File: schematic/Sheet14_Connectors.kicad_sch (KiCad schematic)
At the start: 5 parts, among them J2 JESD_DEBUG, J3 SPW_PORT1, J4 SPW_PORT2, J5 JTAG, J6 SPI_DEBUG

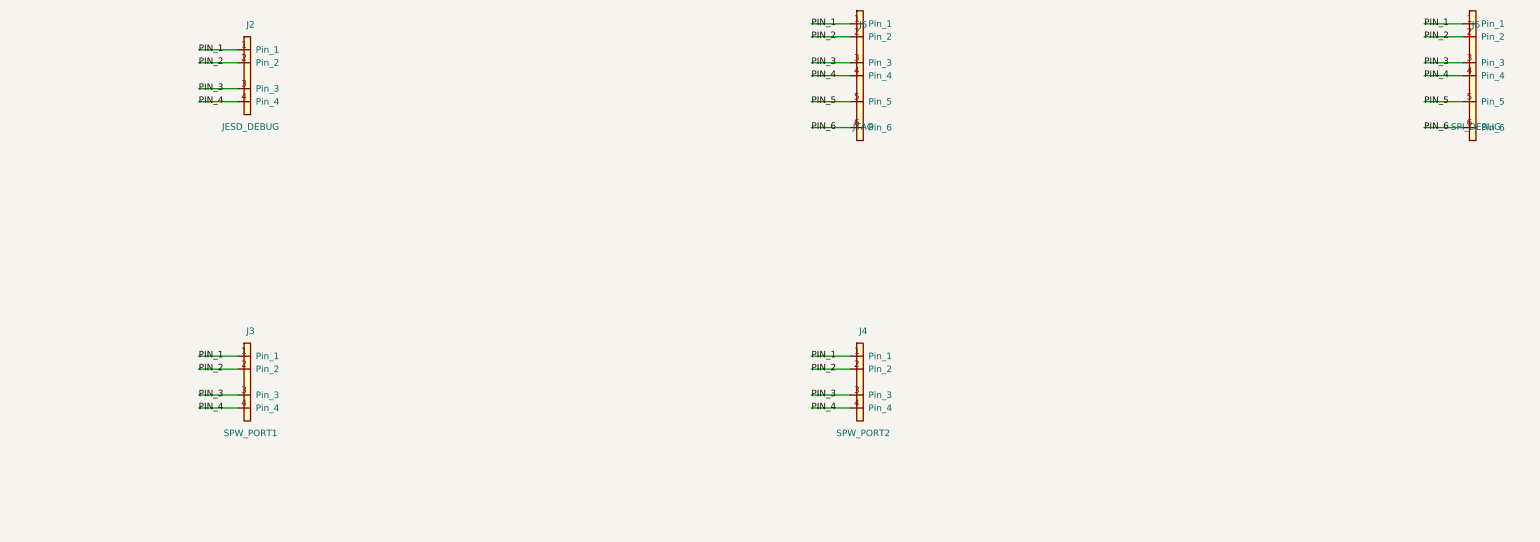
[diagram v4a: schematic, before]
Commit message: fix: replace wire stubs with labels-only to prevent power net shorts
Labels placed directly at pin endpoints eliminate wire overlap that
caused BGA power pins (VA11, VA19, VD11, AGND, DGND) to merge into
a single net. Verified via netlist: GND=52, +1V0_ANA=12, +1V9_ANA=12,
+1V1_DIG=10 nodes (all correct per datasheet pin mapping).
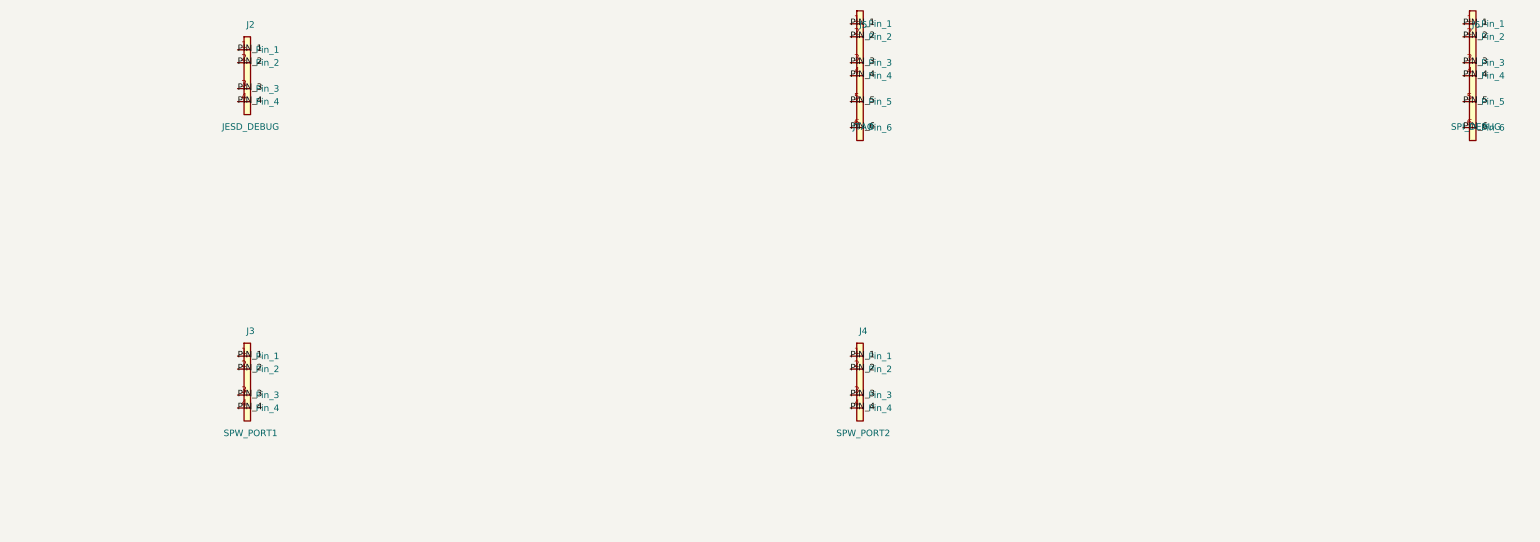
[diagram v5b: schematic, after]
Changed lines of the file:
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@@
     (pin "6")
   )
-  (wire (pts (xy 77.4600 54.9200) (xy 69.8400 54.9200)) (stroke (width 0) (type default)))
-  (label "PIN_1" (at 69.8400 54.9200 0) (effects (font (size 1.27 1.27))))
-  (wire (pts (xy 77.4600 57.4600) (xy 69.8400 57.4600)) (stroke (width 0) (type default)))
-  (label "PIN_2" (at 69.8400 57.4600 0) (effects (font (size 1.27 1.27))))
-  (wire (pts (xy 77.4600 62.5400) (xy 69.8400 62.5400)) (stroke (width 0) (type default)))
-  (label "PIN_3" (at 69.8400 62.5400 0) (effects (font (size 1.27 1.27))))
-  (wire (pts (xy 77.4600 65.0800) (xy 69.8400 65.0800)) (stroke (width 0) (type default)))
-  (label "PIN_4" (at 69.8400 65.0800 0) (effects (font (size 1.27 1.27))))
-  (wire (pts (xy 77.4600 114.9200) (xy 69.8400 114.9200)) (stroke (width 0) (type default)))
-  (label "PIN_1" (at 69.8400 114.9200 0) (effects (font (size 1.27 1.27))))
-  (wire (pts (xy 77.4600 117.4600) (xy 69.8400 117.4600)) (stroke (width 0) (type default)))
-  (label "PIN_2" (at 69.8400 117.4600 0) (effects (font (size 1.27 1.27))))
-  (wire (pts (xy 77.4600 122.5400) (xy 69.8400 122.5400)) (stroke (width 0) (type default)))
-  (label "PIN_3" (at 69.8400 122.5400 0) (effects (font (size 1.27 1.27))))
-  (wire (pts (xy 77.4600 125.0800) (xy 69.8400 125.0800)) (stroke (width 0) (type default)))
-  (label "PIN_4" (at 69.8400 125.0800 0) (effects (font (size 1.27 1.27))))
-  (wire (pts (xy 197.4600 114.9200) (xy 189.8400 114.9200)) (stroke (width 0) (type default)))
-  (label "PIN_1" (at 189.8400 114.9200 0) (effects (font (size 1.27 1.27))))
-  (wire (pts (xy 197.4600 117.4600) (xy 189.8400 117.4600)) (stroke (width 0) (type default)))
-  (label "PIN_2" (at 189.8400 117.4600 0) (effects (font (size 1.27 1.27))))
-  (wire (pts (xy 197.4600 122.5400) (xy 189.8400 122.5400)) (stroke (width 0) (type default)))
-  (label "PIN_3" (at 189.8400 122.5400 0) (effects (font (size 1.27 1.27))))
-  (wire (pts (xy 197.4600 125.0800) (xy 189.8400 125.0800)) (stroke (width 0) (type default)))
-  (label "PIN_4" (at 189.8400 125.0800 0) (effects (font (size 1.27 1.27))))
-  (wire (pts (xy 197.4600 49.8400) (xy 189.8400 49.8400)) (stroke (width 0) (type default)))
-  (label "PIN_1" (at 189.8400 49.8400 0) (effects (font (size 1.27 1.27))))
-  (wire (pts (xy 197.4600 52.3800) (xy 189.8400 52.3800)) (stroke (width 0) (type default)))
-  (label "PIN_2" (at 189.8400 52.3800 0) (effects (font (size 1.27 1.27))))
-  (wire (pts (xy 197.4600 57.4600) (xy 189.8400 57.4600)) (stroke (width 0) (type default)))
-  (label "PIN_3" (at 189.8400 57.4600 0) (effects (font (size 1.27 1.27))))
-  (wire (pts (xy 197.4600 60.0000) (xy 189.8400 60.0000)) (stroke (width 0) (type default)))
-  (label "PIN_4" (at 189.8400 60.0000 0) (effects (font (size 1.27 1.27))))
-  (wire (pts (xy 197.4600 65.0800) (xy 189.8400 65.0800)) (stroke (width 0) (type default)))
-  (label "PIN_5" (at 189.8400 65.0800 0) (effects (font (size 1.27 1.27))))
-  (wire (pts (xy 197.4600 70.1600) (xy 189.8400 70.1600)) (stroke (width 0) (type default)))
-  (label "PIN_6" (at 189.8400 70.1600 0) (effects (font (size 1.27 1.27))))
-  (wire (pts (xy 317.4600 49.8400) (xy 309.8400 49.8400)) (stroke (width 0) (type default)))
-  (label "PIN_1" (at 309.8400 49.8400 0) (effects (font (size 1.27 1.27))))
-  (wire (pts (xy 317.4600 52.3800) (xy 309.8400 52.3800)) (stroke (width 0) (type default)))
-  (label "PIN_2" (at 309.8400 52.3800 0) (effects (font (size 1.27 1.27))))
-  (wire (pts (xy 317.4600 57.4600) (xy 309.8400 57.4600)) (stroke (width 0) (type default)))
-  (label "PIN_3" (at 309.8400 57.4600 0) (effects (font (size 1.27 1.27))))
-  (wire (pts (xy 317.4600 60.0000) (xy 309.8400 60.0000)) (stroke (width 0) (type default)))
-  (label "PIN_4" (at 309.8400 60.0000 0) (effects (font (size 1.27 1.27))))
-  (wire (pts (xy 317.4600 65.0800) (xy 309.8400 65.0800)) (stroke (width 0) (type default)))
-  (label "PIN_5" (at 309.8400 65.0800 0) (effects (font (size 1.27 1.27))))
-  (wire (pts (xy 317.4600 70.1600) (xy 309.8400 70.1600)) (stroke (width 0) (type default)))
-  (label "PIN_6" (at 309.8400 70.1600 0) (effects (font (size 1.27 1.27))))
+  (label "PIN_1" (at 77.4600 54.9200 0) (effects (font (size 1.27 1.27))))
+  (label "PIN_2" (at 77.4600 57.4600 0) (effects (font (size 1.27 1.27))))
+  (label "PIN_3" (at 77.4600 62.5400 0) (effects (font (size 1.27 1.27))))
+  (label "PIN_4" (at 77.4600 65.0800 0) (effects (font (size 1.27 1.27))))
+  (label "PIN_1" (at 77.4600 114.9200 0) (effects (font (size 1.27 1.27))))
+  (label "PIN_2" (at 77.4600 117.4600 0) (effects (font (size 1.27 1.27))))
+  (label "PIN_3" (at 77.4600 122.5400 0) (effects (font (size 1.27 1.27))))
+  (label "PIN_4" (at 77.4600 125.0800 0) (effects (font (size 1.27 1.27))))
+  (label "PIN_1" (at 197.4600 114.9200 0) (effects (font (size 1.27 1.27))))
+  (label "PIN_2" (at 197.4600 117.4600 0) (effects (font (size 1.27 1.27))))
+  (label "PIN_3" (at 197.4600 122.5400 0) (effects (font (size 1.27 1.27))))
+  (label "PIN_4" (at 197.4600 125.0800 0) (effects (font (size 1.27 1.27))))
+  (label "PIN_1" (at 197.4600 49.8400 0) (effects (font (size 1.27 1.27))))
+  (label "PIN_2" (at 197.4600 52.3800 0) (effects (font (size 1.27 1.27))))
+  (label "PIN_3" (at 197.4600 57.4600 0) (effects (font (size 1.27 1.27))))
+  (label "PIN_4" (at 197.4600 60.0000 0) (effects (font (size 1.27 1.27))))
+  (label "PIN_5" (at 197.4600 65.0800 0) (effects (font (size 1.27 1.27))))
+  (label "PIN_6" (at 197.4600 70.1600 0) (effects (font (size 1.27 1.27))))
+  (label "PIN_1" (at 317.4600 49.8400 0) (effects (font (size 1.27 1.27))))
+  (label "PIN_2" (at 317.4600 52.3800 0) (effects (font (size 1.27 1.27))))
+  (label "PIN_3" (at 317.4600 57.4600 0) (effects (font (size 1.27 1.27))))
+  (label "PIN_4" (at 317.4600 60.0000 0) (effects (font (size 1.27 1.27))))
+  (label "PIN_5" (at 317.4600 65.0800 0) (effects (font (size 1.27 1.27))))
+  (label "PIN_6" (at 317.4600 70.1600 0) (effects (font (size 1.27 1.27))))
   (sheet_instances (path "/" (page "1")))
 )

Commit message: fix: isolate ISL70003ASEH buck pins, fix LMX_SYNC collision, NC pins, connector pin names
- ISL70003ASEH pins now use ref prefix (U6_LX1 vs U7_LX1) to prevent shorts
- Buck SYNC pins separated from LMX_SYNC (power sync ≠ PLL sync)
- NC pins properly skipped (unconnected)
- Connector PIN_1..PIN_6 use ref prefix (J1_PIN_1 vs J2_PIN_1)
- Fixed annotation warnings in Sheet13 (C_dev→C125, R_dev→R74, U_TPS7H→U14)
- Regenerated all PDFs and SVGs
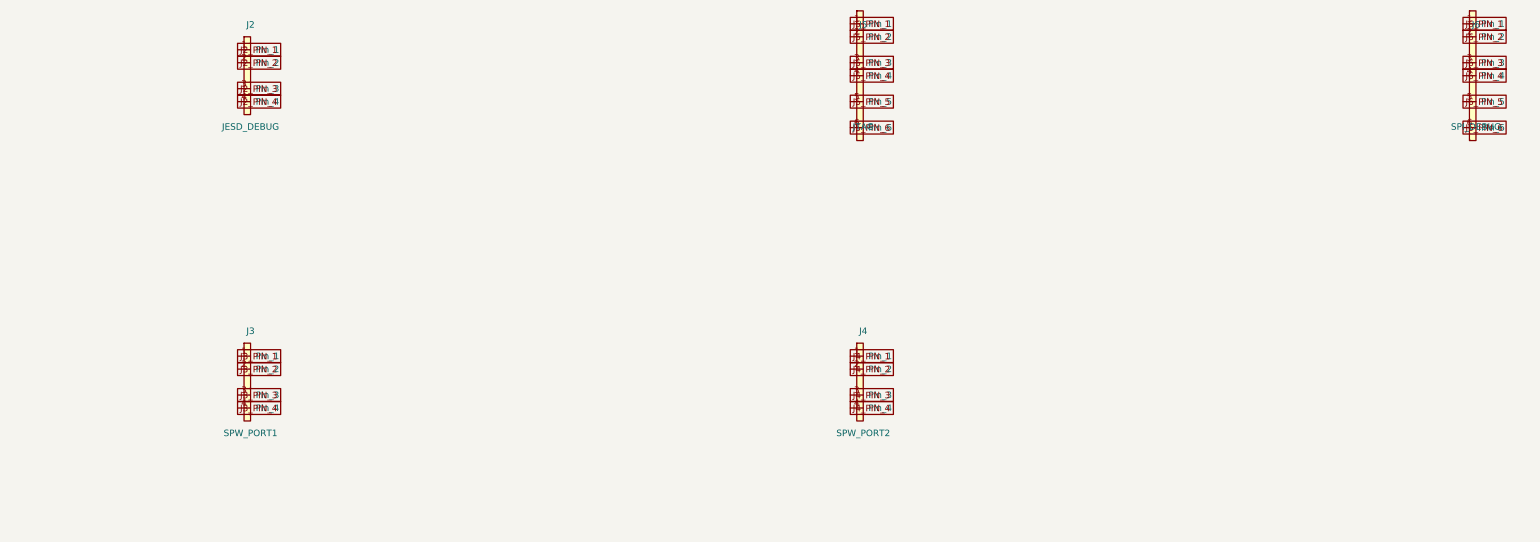
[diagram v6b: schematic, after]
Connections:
- removed net PIN_1: J2.1 (Pin_1), J3.1 (Pin_1), J4.1 (Pin_1), J5.1 (Pin_1), J6.1 (Pin_1)
- removed net PIN_2: J2.2 (Pin_2), J3.2 (Pin_2), J4.2 (Pin_2), J5.2 (Pin_2), J6.2 (Pin_2)
- removed net PIN_3: J2.3 (Pin_3), J3.3 (Pin_3), J4.3 (Pin_3), J5.3 (Pin_3), J6.3 (Pin_3)
- removed net PIN_4: J2.4 (Pin_4), J3.4 (Pin_4), J4.4 (Pin_4), J5.4 (Pin_4), J6.4 (Pin_4)
- net PIN_5 renamed J5_PIN_5
- net J5_PIN_5: no longer J6.5 (Pin_5)
- net PIN_6 renamed J5_PIN_6
- net J5_PIN_6: no longer J6.6 (Pin_6)
- new net J2_PIN_1: J2.1 (Pin_1)
- new net J2_PIN_2: J2.2 (Pin_2)
- new net J2_PIN_3: J2.3 (Pin_3)
- new net J2_PIN_4: J2.4 (Pin_4)
- new net J3_PIN_1: J3.1 (Pin_1)
- new net J3_PIN_2: J3.2 (Pin_2)
- new net J3_PIN_3: J3.3 (Pin_3)
- new net J3_PIN_4: J3.4 (Pin_4)
- new net J4_PIN_1: J4.1 (Pin_1)
- new net J4_PIN_2: J4.2 (Pin_2)
- new net J4_PIN_3: J4.3 (Pin_3)
- new net J4_PIN_4: J4.4 (Pin_4)
- new net J5_PIN_1: J5.1 (Pin_1)
- new net J5_PIN_2: J5.2 (Pin_2)
- new net J5_PIN_3: J5.3 (Pin_3)
- new net J5_PIN_4: J5.4 (Pin_4)
- new net J6_PIN_1: J6.1 (Pin_1)
- new net J6_PIN_2: J6.2 (Pin_2)
- new net J6_PIN_3: J6.3 (Pin_3)
- new net J6_PIN_4: J6.4 (Pin_4)
- new net J6_PIN_5: J6.5 (Pin_5)
- new net J6_PIN_6: J6.6 (Pin_6)
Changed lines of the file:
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@@
     (pin "6")
   )
-  (label "PIN_1" (at 77.4600 54.9200 0) (effects (font (size 1.27 1.27))))
-  (label "PIN_2" (at 77.4600 57.4600 0) (effects (font (size 1.27 1.27))))
-  (label "PIN_3" (at 77.4600 62.5400 0) (effects (font (size 1.27 1.27))))
-  (label "PIN_4" (at 77.4600 65.0800 0) (effects (font (size 1.27 1.27))))
-  (label "PIN_1" (at 77.4600 114.9200 0) (effects (font (size 1.27 1.27))))
-  (label "PIN_2" (at 77.4600 117.4600 0) (effects (font (size 1.27 1.27))))
-  (label "PIN_3" (at 77.4600 122.5400 0) (effects (font (size 1.27 1.27))))
-  (label "PIN_4" (at 77.4600 125.0800 0) (effects (font (size 1.27 1.27))))
-  (label "PIN_1" (at 197.4600 114.9200 0) (effects (font (size 1.27 1.27))))
-  (label "PIN_2" (at 197.4600 117.4600 0) (effects (font (size 1.27 1.27))))
-  (label "PIN_3" (at 197.4600 122.5400 0) (effects (font (size 1.27 1.27))))
-  (label "PIN_4" (at 197.4600 125.0800 0) (effects (font (size 1.27 1.27))))
-  (label "PIN_1" (at 197.4600 49.8400 0) (effects (font (size 1.27 1.27))))
-  (label "PIN_2" (at 197.4600 52.3800 0) (effects (font (size 1.27 1.27))))
-  (label "PIN_3" (at 197.4600 57.4600 0) (effects (font (size 1.27 1.27))))
-  (label "PIN_4" (at 197.4600 60.0000 0) (effects (font (size 1.27 1.27))))
-  (label "PIN_5" (at 197.4600 65.0800 0) (effects (font (size 1.27 1.27))))
-  (label "PIN_6" (at 197.4600 70.1600 0) (effects (font (size 1.27 1.27))))
-  (label "PIN_1" (at 317.4600 49.8400 0) (effects (font (size 1.27 1.27))))
-  (label "PIN_2" (at 317.4600 52.3800 0) (effects (font (size 1.27 1.27))))
-  (label "PIN_3" (at 317.4600 57.4600 0) (effects (font (size 1.27 1.27))))
-  (label "PIN_4" (at 317.4600 60.0000 0) (effects (font (size 1.27 1.27))))
-  (label "PIN_5" (at 317.4600 65.0800 0) (effects (font (size 1.27 1.27))))
-  (label "PIN_6" (at 317.4600 70.1600 0) (effects (font (size 1.27 1.27))))
+  (global_label "J2_PIN_1" (at 77.4600 54.9200 0) (effects (font (size 1.27 1.27))))
+  (global_label "J2_PIN_2" (at 77.4600 57.4600 0) (effects (font (size 1.27 1.27))))
+  (global_label "J2_PIN_3" (at 77.4600 62.5400 0) (effects (font (size 1.27 1.27))))
+  (global_label "J2_PIN_4" (at 77.4600 65.0800 0) (effects (font (size 1.27 1.27))))
+  (global_label "J3_PIN_1" (at 77.4600 114.9200 0) (effects (font (size 1.27 1.27))))
+  (global_label "J3_PIN_2" (at 77.4600 117.4600 0) (effects (font (size 1.27 1.27))))
+  (global_label "J3_PIN_3" (at 77.4600 122.5400 0) (effects (font (size 1.27 1.27))))
+  (global_label "J3_PIN_4" (at 77.4600 125.0800 0) (effects (font (size 1.27 1.27))))
+  (global_label "J4_PIN_1" (at 197.4600 114.9200 0) (effects (font (size 1.27 1.27))))
+  (global_label "J4_PIN_2" (at 197.4600 117.4600 0) (effects (font (size 1.27 1.27))))
+  (global_label "J4_PIN_3" (at 197.4600 122.5400 0) (effects (font (size 1.27 1.27))))
+  (global_label "J4_PIN_4" (at 197.4600 125.0800 0) (effects (font (size 1.27 1.27))))
+  (global_label "J5_PIN_1" (at 197.4600 49.8400 0) (effects (font (size 1.27 1.27))))
+  (global_label "J5_PIN_2" (at 197.4600 52.3800 0) (effects (font (size 1.27 1.27))))
+  (global_label "J5_PIN_3" (at 197.4600 57.4600 0) (effects (font (size 1.27 1.27))))
+  (global_label "J5_PIN_4" (at 197.4600 60.0000 0) (effects (font (size 1.27 1.27))))
+  (global_label "J5_PIN_5" (at 197.4600 65.0800 0) (effects (font (size 1.27 1.27))))
+  (global_label "J5_PIN_6" (at 197.4600 70.1600 0) (effects (font (size 1.27 1.27))))
+  (global_label "J6_PIN_1" (at 317.4600 49.8400 0) (effects (font (size 1.27 1.27))))
+  (global_label "J6_PIN_2" (at 317.4600 52.3800 0) (effects (font (size 1.27 1.27))))
+  (global_label "J6_PIN_3" (at 317.4600 57.4600 0) (effects (font (size 1.27 1.27))))
+  (global_label "J6_PIN_4" (at 317.4600 60.0000 0) (effects (font (size 1.27 1.27))))
+  (global_label "J6_PIN_5" (at 317.4600 65.0800 0) (effects (font (size 1.27 1.27))))
+  (global_label "J6_PIN_6" (at 317.4600 70.1600 0) (effects (font (size 1.27 1.27))))
   (sheet_instances (path "/" (page "1")))
 )
